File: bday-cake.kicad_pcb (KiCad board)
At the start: 2 copper layers, 566.9 x 566.9 mm, 0 parts

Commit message: update layout
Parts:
- added BAT1: BATTERY-CR1220-3V-COIN, Wickerlib:BATT-HOLDER-CR1220-BK-916, F.Cu at (140.7, 159.0)
- added D1: LED, LED_THT:LED_D5.0mm, F.Cu at (148.3, 136.1)
- added R1: R, Resistor_THT:R_Axial_DIN0207_L6.3mm_D2.5mm_P2.54mm_Vertical, F.Cu at (130.9, 136.0)
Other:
- board size 566.9 x 566.9 mm -> 165.1 x 165.1 mm
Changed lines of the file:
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@@
   (general
     (thickness 1.6)
-    (drawings 38)
+    (drawings 34)
     (tracks 0)
     (zones 0)
-    (modules 0)
-    (nets 1)
+    (modules 3)
+    (nets 4)
   )
   (page A4)
@@
   )
   (net 0 "")
+  (net 1 "Net-(D1-Pad1)")
+  (net 2 "Net-(D1-Pad2)")
+  (net 3 "Net-(R1-Pad2)")
   (net_class Default "This is the default net class."
     (clearance 0.2)
@@
     (uvia_dia 0.3)
     (uvia_drill 0.1)
+    (add_net "Net-(D1-Pad1)")
+    (add_net "Net-(D1-Pad2)")
+    (add_net "Net-(R1-Pad2)")
+  )
+  (module Wickerlib:BATT-HOLDER-CR1220-BK-916 (layer F.Cu)
+    (at 140.686 159.0294)
+    (attr smd)
+    (fp_text reference BAT1 (at 0 0) (layer F.Fab)
+      (effects (font (size 2 2) (thickness 0.254)))
+    )
+    (fp_text value BATTERY-CR1220-3V-COIN (at 0 2) (layer F.Fab) hide
+      (effects (font (size 1 1) (thickness 0.15)))
+    )
+    (fp_line (start 9.1948 4.6228) (end 4.9022 4.6228) (layer F.Fab) (width 0.049784))
+    (fp_line (start 9.1948 -4.6482) (end 9.1948 4.6228) (layer F.Fab) (width 0.049784))
+    (fp_line (start 4.6736 -4.6482) (end 9.1948 -4.6482) (layer F.Fab) (width 0.049784))
+    (fp_line (start -7.75 -4.5) (end -7.75 -3) (layer F.SilkS) (width 0.1524))
+    (fp_line (start -4.5 -4.5) (end -7.75 -4.5) (layer F.SilkS) (width 0.1524))
+    (fp_line (start 8 -4.5) (end 8 -3) (layer F.SilkS) (width 0.1524))
+    (fp_line (start 7.75 -4.5) (end 8 -4.5) (layer F.SilkS) (width 0.1524))
+    (fp_line (start 4.5 -4.5) (end 7.75 -4.5) (layer F.SilkS) (width 0.1524))
+    (fp_arc (start 0 0.25) (end -4.5 -4.5) (angle 86.47690829) (layer F.SilkS) (width 0.1524))
+    (fp_text user %R (at -6.25 -5.75) (layer F.SilkS)
+      (effects (font (size 1 1) (thickness 0.15)))
+    )
+    (fp_arc (start 0.25 -0.25) (end 4.75 4.5) (angle 86.47690829) (layer F.SilkS) (width 0.1524))
+    (fp_line (start -4.25 4.5) (end -7.5 4.5) (layer F.SilkS) (width 0.1524))
+    (fp_line (start -7.5 4.5) (end -7.75 4.5) (layer F.SilkS) (width 0.1524))
+    (fp_line (start -7.75 4.5) (end -7.75 3) (layer F.SilkS) (width 0.1524))
+    (fp_line (start 4.75 4.5) (end 8 4.5) (layer F.SilkS) (width 0.1524))
+    (fp_line (start 8 4.5) (end 8 3) (layer F.SilkS) (width 0.1524))
+    (fp_arc (start 0 0.25) (end -4.6 -4.7) (angle 86.44924622) (layer F.Fab) (width 0.0508))
+    (fp_arc (start 0.261407 -0.300336) (end 4.9022 4.6228) (angle 86.8571776) (layer F.Fab) (width 0.0508))
+    (fp_line (start -4.399893 4.603389) (end -9.2964 4.5974) (layer F.Fab) (width 0.049784))
+    (fp_line (start -9.2964 4.5974) (end -9.2964 -4.699) (layer F.Fab) (width 0.049784))
+    (fp_line (start -9.2964 -4.699) (end -4.5974 -4.699) (layer F.Fab) (width 0.049784))
+    (pad 1 smd rect (at 7.65 0) (size 2.5 5.1) (layers F.Cu F.Paste F.Mask))
+    (pad 1 smd rect (at -7.65 0) (size 2.5 5.1) (layers F.Cu F.Paste F.Mask))
+    (pad GND smd circle (at 0 0) (size 10.2 10.2) (layers F.Cu F.Mask))
+  )
+  (module LED_THT:LED_D5.0mm (layer F.Cu)
+    (at 148.3106 136.0678)
+    (descr "LED, diameter 5.0mm, 2 pins, http://cdn-reichelt.de/documents/datenblatt/A500/LL-504BC2E-009.pdf")
+    (tags "LED diameter 5.0mm 2 pins")
+    (fp_text reference D1 (at 1.27 -3.96) (layer F.SilkS)
+      (effects (font (size 1 1) (thickness 0.15)))
+    )
+    (fp_text value LED (at 1.27 3.96) (layer F.Fab)
+      (effects (font (size 1 1) (thickness 0.15)))
+    )
+    (fp_arc (start 1.27 0) (end -1.23 -1.469694) (angle 299.1) (layer F.Fab) (width 0.1))
+    (fp_arc (start 1.27 0) (end -1.29 -1.54483) (angle 148.9) (layer F.SilkS) (width 0.12))
+    (fp_arc (start 1.27 0) (end -1.29 1.54483) (angle -148.9) (layer F.SilkS) (width 0.12))
+    (fp_circle (center 1.27 0) (end 3.77 0) (layer F.Fab) (width 0.1))
+    (fp_circle (center 1.27 0) (end 3.77 0) (layer F.SilkS) (width 0.12))
+    (fp_line (start -1.23 -1.469694) (end -1.23 1.469694) (layer F.Fab) (width 0.1))
+    (fp_line (start -1.29 -1.545) (end -1.29 1.545) (layer F.SilkS) (width 0.12))
+    (fp_line (start -1.95 -3.25) (end -1.95 3.25) (layer F.CrtYd) (width 0.05))
+    (fp_line (start -1.95 3.25) (end 4.5 3.25) (layer F.CrtYd) (width 0.05))
+    (fp_line (start 4.5 3.25) (end 4.5 -3.25) (layer F.CrtYd) (width 0.05))
+    (fp_line (start 4.5 -3.25) (end -1.95 -3.25) (layer F.CrtYd) (width 0.05))
+    (fp_text user %R (at 1.25 0) (layer F.Fab)
+      (effects (font (size 0.8 0.8) (thickness 0.2)))
+    )
+    (pad 1 thru_hole rect (at 0 0) (size 1.8 1.8) (drill 0.9) (layers *.Cu *.Mask)
+      (net 1 "Net-(D1-Pad1)"))
+    (pad 2 thru_hole circle (at 2.54 0) (size 1.8 1.8) (drill 0.9) (layers *.Cu *.Mask)
+      (net 2 "Net-(D1-Pad2)"))
+    (model ${KISYS3DMOD}/LED_THT.3dshapes/LED_D5.0mm.wrl
+      (at (xyz 0 0 0))
+      (scale (xyz 1 1 1))
+      (rotate (xyz 0 0 0))
+    )
+  )
+  (module Resistor_THT:R_Axial_DIN0207_L6.3mm_D2.5mm_P2.54mm_Vertical (layer F.Cu)
+    (at 130.9116 136.017)
+    (descr "Resistor, Axial_DIN0207 series, Axial, Vertical, pin pitch=2.54mm, 0.25W = 1/4W, length*diameter=6.3*2.5mm^2, http://cdn-reichelt.de/documents/datenblatt/B400/1_4W%23YAG.pdf")
+    (tags "Resistor Axial_DIN0207 series Axial Vertical pin pitch 2.54mm 0.25W = 1/4W length 6.3mm diameter 2.5mm")
+    (fp_text reference R1 (at 1.27 -2.37) (layer F.SilkS)
+      (effects (font (size 1 1) (thickness 0.15)))
+    )
+    (fp_text value R (at 1.27 2.37) (layer F.Fab)
+      (effects (font (size 1 1) (thickness 0.15)))
+    )
+    (fp_circle (center 0 0) (end 1.25 0) (layer F.Fab) (width 0.1))
+    (fp_circle (center 0 0) (end 1.37 0) (layer F.SilkS) (width 0.12))
+    (fp_line (start 0 0) (end 2.54 0) (layer F.Fab) (width 0.1))
+    (fp_line (start 1.37 0) (end 1.44 0) (layer F.SilkS) (width 0.12))
+    (fp_line (start -1.5 -1.5) (end -1.5 1.5) (layer F.CrtYd) (width 0.05))
+    (fp_line (start -1.5 1.5) (end 3.59 1.5) (layer F.CrtYd) (width 0.05))
+    (fp_line (start 3.59 1.5) (end 3.59 -1.5) (layer F.CrtYd) (width 0.05))
+    (fp_line (start 3.59 -1.5) (end -1.5 -1.5) (layer F.CrtYd) (width 0.05))
+    (fp_text user %R (at 1.27 -2.37) (layer F.Fab)
+      (effects (font (size 1 1) (thickness 0.15)))
+    )
+    (pad 1 thru_hole circle (at 0 0) (size 1.6 1.6) (drill 0.8) (layers *.Cu *.Mask)
+      (net 1 "Net-(D1-Pad1)"))
+    (pad 2 thru_hole oval (at 2.54 0) (size 1.6 1.6) (drill 0.8) (layers *.Cu *.Mask)
+      (net 3 "Net-(R1-Pad2)"))
+    (model ${KISYS3DMOD}/Resistor_THT.3dshapes/R_Axial_DIN0207_L6.3mm_D2.5mm_P2.54mm_Vertical.wrl
+      (at (xyz 0 0 0))
+      (scale (xyz 1 1 1))
+      (rotate (xyz 0 0 0))
+    )
   )
   (gr_line (start 143.031577 39.308707) (end 143.031577 39.308707) (layer Edge.Cuts) (width 0.2))
@@
   (gr_curve (pts (xy 63.130208 181.279896) (xy 61.675471 181.279896) (xy 60.496426 182.458948) (xy 60.496426 183.913686)) (layer Edge.Cuts) (width 0.2))
   (gr_line (start 133.373865 103.836539) (end 90.15804 103.836539) (layer Edge.Cuts) (width 0.2))
-  (gr_line (start -125.862462 465.088428) (end -125.862462 -101.840706) (layer Edge.Cuts) (width 0.2))
-  (gr_line (start 441.066672 465.088428) (end -125.862462 465.088428) (layer Edge.Cuts) (width 0.2))
   (gr_line (start 133.373865 79.886339) (end 133.373865 103.836539) (layer Edge.Cuts) (width 0.2))
   (gr_curve (pts (xy 90.15804 103.836539) (xy 80.959335 103.836539) (xy 73.476405 111.320939) (xy 73.476405 120.519644)) (layer Edge.Cuts) (width 0.2))
@@
   (gr_curve (pts (xy 141.97689 33.988395) (xy 132.732885 38.028435) (xy 126.276697 46.79601) (xy 126.276697 55.30773)) (layer Edge.Cuts) (width 0.2))
   (gr_curve (pts (xy 137.856285 73.974232) (xy 135.273756 74.702062) (xy 133.373865 77.074319) (xy 133.373865 79.886339)) (layer Edge.Cuts) (width 0.2))
-  (gr_line (start -125.862462 -101.840706) (end 441.066672 -101.840706) (layer Edge.Cuts) (width 0.2))
-  (gr_line (start 441.066672 -101.840706) (end 441.066672 465.088428) (layer Edge.Cuts) (width 0.2))
   (gr_curve (pts (xy 126.276697 55.30773) (xy 126.276697 59.419065) (xy 127.787602 63.374317) (xy 130.5306 66.4464)) (layer Edge.Cuts) (width 0.2))
   (gr_curve (pts (xy 130.5306 66.4464) (xy 130.883632 66.842332) (xy 134.999685 71.192767) (xy 137.856285 73.974232)) (layer Edge.Cuts) (width 0.2))

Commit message: update layout
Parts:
- removed BAT1: BATTERY-CR1220-3V-COIN, Wickerlib:BATT-HOLDER-CR1220-BK-916
- added BT1: Battery_Cell, Battery:BatteryHolder_Keystone_3002_1x2032, F.Cu at (174.0, -73.7)
- added S1: SWITCH-TACTILE-SPST-NO-0.05A-24V-SMT-FSMSMTR, Wickerlib:SWITCH-ESWITCH-SLIDE-TH-EG1218, F.Cu at (144.8, -64.8)
- R1: footprint Resistor_THT:R_Axial_DIN0207_L6.3mm_D2.5mm_P2.54mm_Vertical -> Resistor_THT:R_Axial_DIN0207_L6.3mm_D2.5mm_P7.62mm_Horizontal
- moved D1 290.9 mm to (174.0, -153.7)
- moved R1 215.1 mm to (143.5, -78.7), turned to 270 degrees
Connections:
- D1 pad 2: Net-(D1-Pad2) -> +3V3
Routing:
- net Net-(D1-Pad1): track 0.00 -> 88.1 mm
- net GND: track 0.00 -> 46.8 mm
- net Net-(R1-Pad2): track 0.00 -> 6.47 mm
- added copper zone on F.Cu, net +3V3
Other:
- board size 165.1 x 165.1 mm -> 108 x 108 mm
- board text added: "Dear Mom,"
- board text added: "Happy Birthday!"
- board text added: "Love, Andrew"

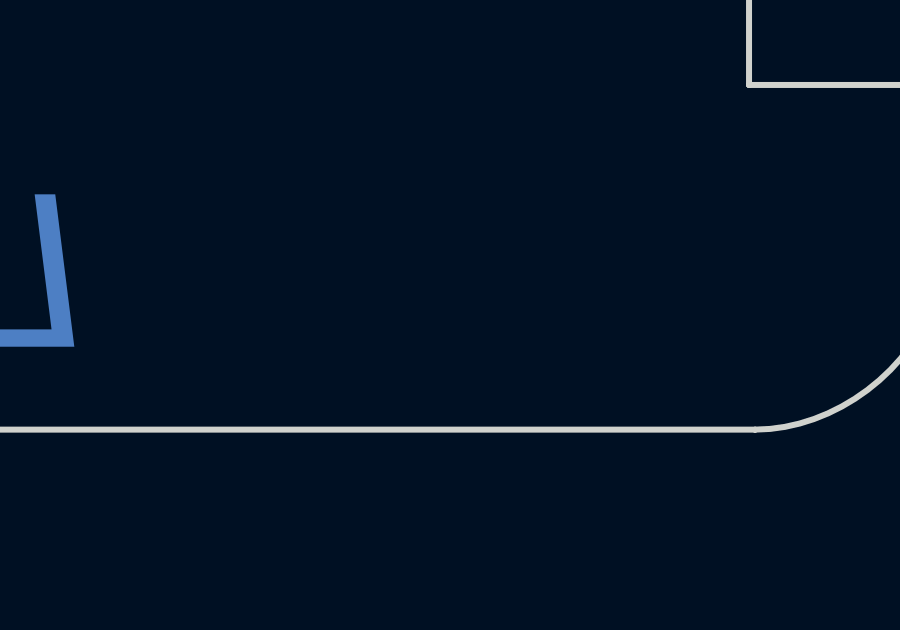
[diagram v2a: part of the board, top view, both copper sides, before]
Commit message: update schematic and layout
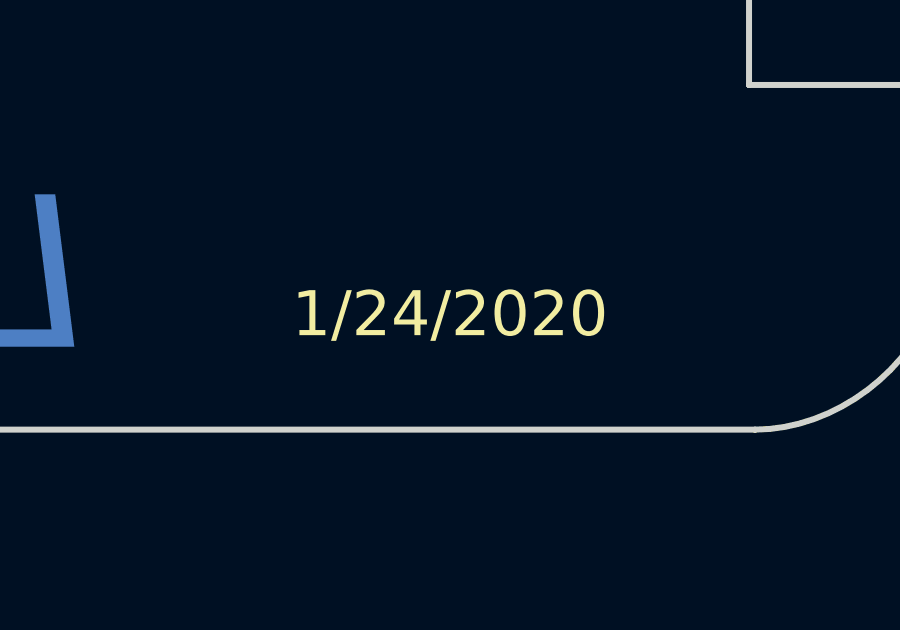
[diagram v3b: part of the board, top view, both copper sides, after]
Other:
- board text added: "1/24/2020"
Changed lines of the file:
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@@
   (general
     (thickness 1.6)
-    (drawings 39)
+    (drawings 40)
     (tracks 55)
     (zones 0)
@@
     )
   )
+  (gr_text "1/24/2020\n" (at 209.55 -62.23) (layer F.SilkS)
+    (effects (font (size 1.5 1.5) (thickness 0.3)))
+  )
   (gr_text "Dear Mom," (at 194.31 -111.76) (layer B.Mask)
